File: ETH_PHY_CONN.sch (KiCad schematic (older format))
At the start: 65 parts, among them J2 RJMG2012211A0FR, U7 DP83869HMRGZT, Y1 XRCGE25M000FBA1AR0

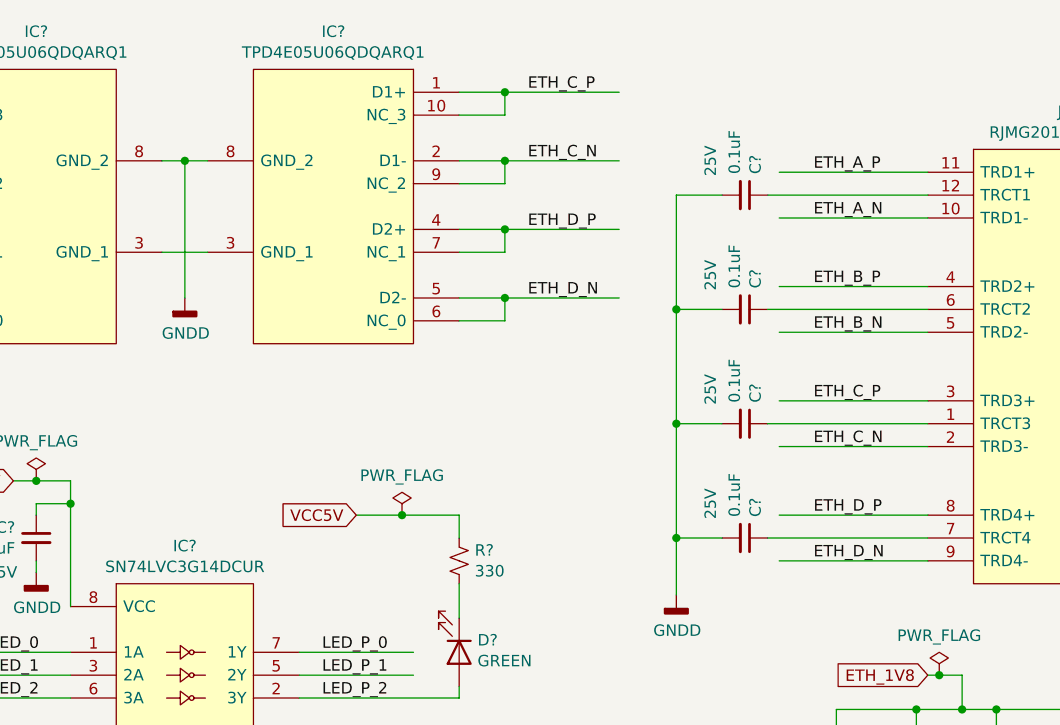
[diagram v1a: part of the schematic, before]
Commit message: Corrected Eth conn connections
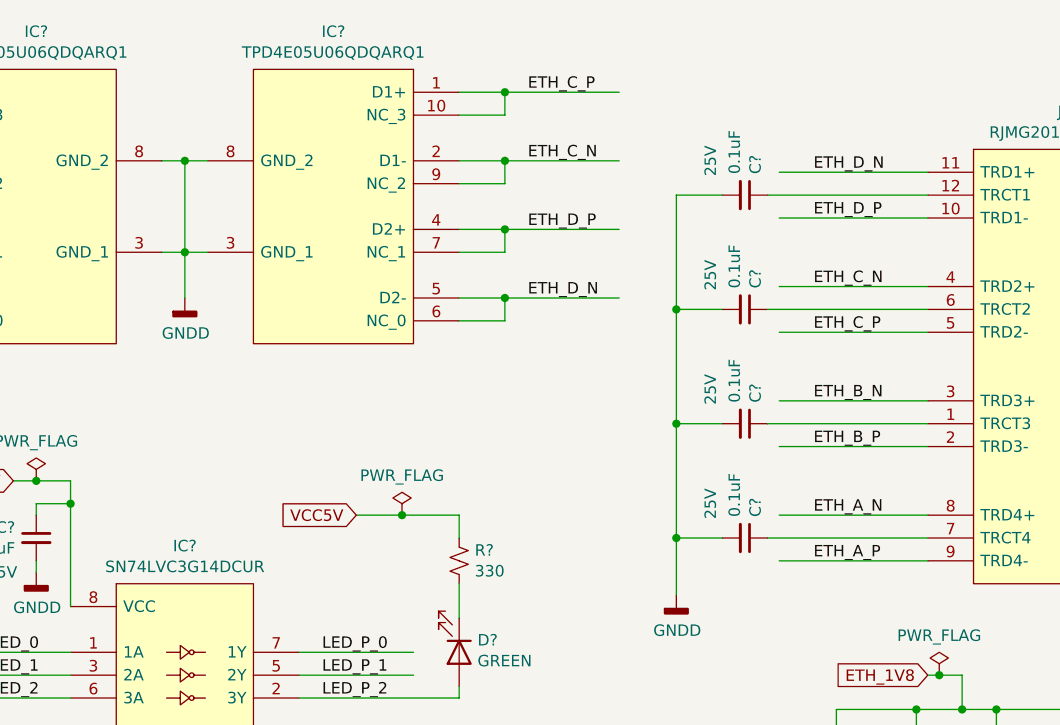
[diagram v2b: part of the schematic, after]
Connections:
- wire segments 304 -> 306

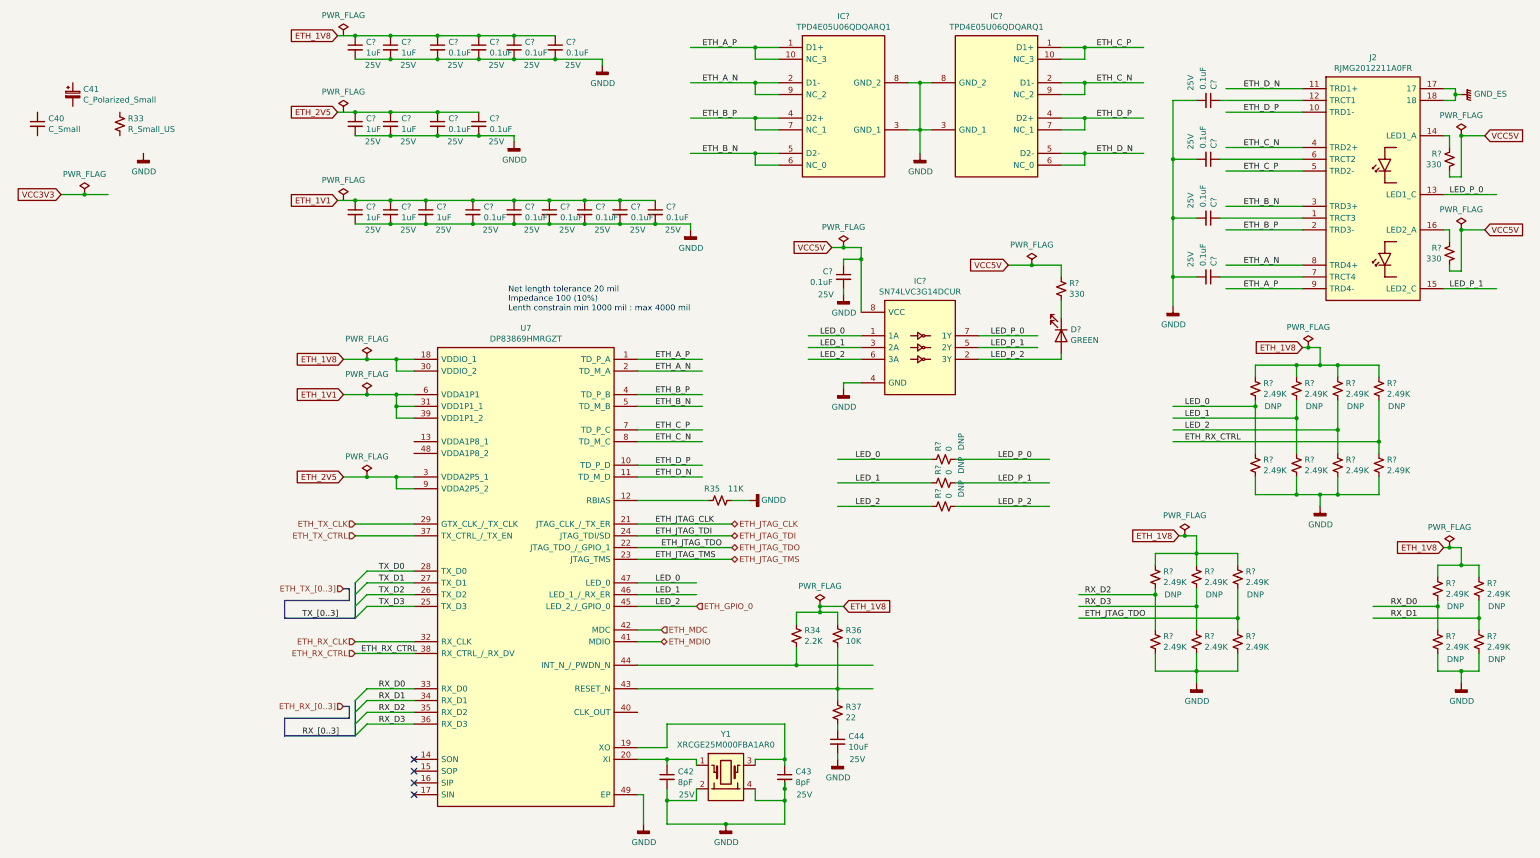
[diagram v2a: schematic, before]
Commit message: Modified LED nets and JTag nets of ETH schematic
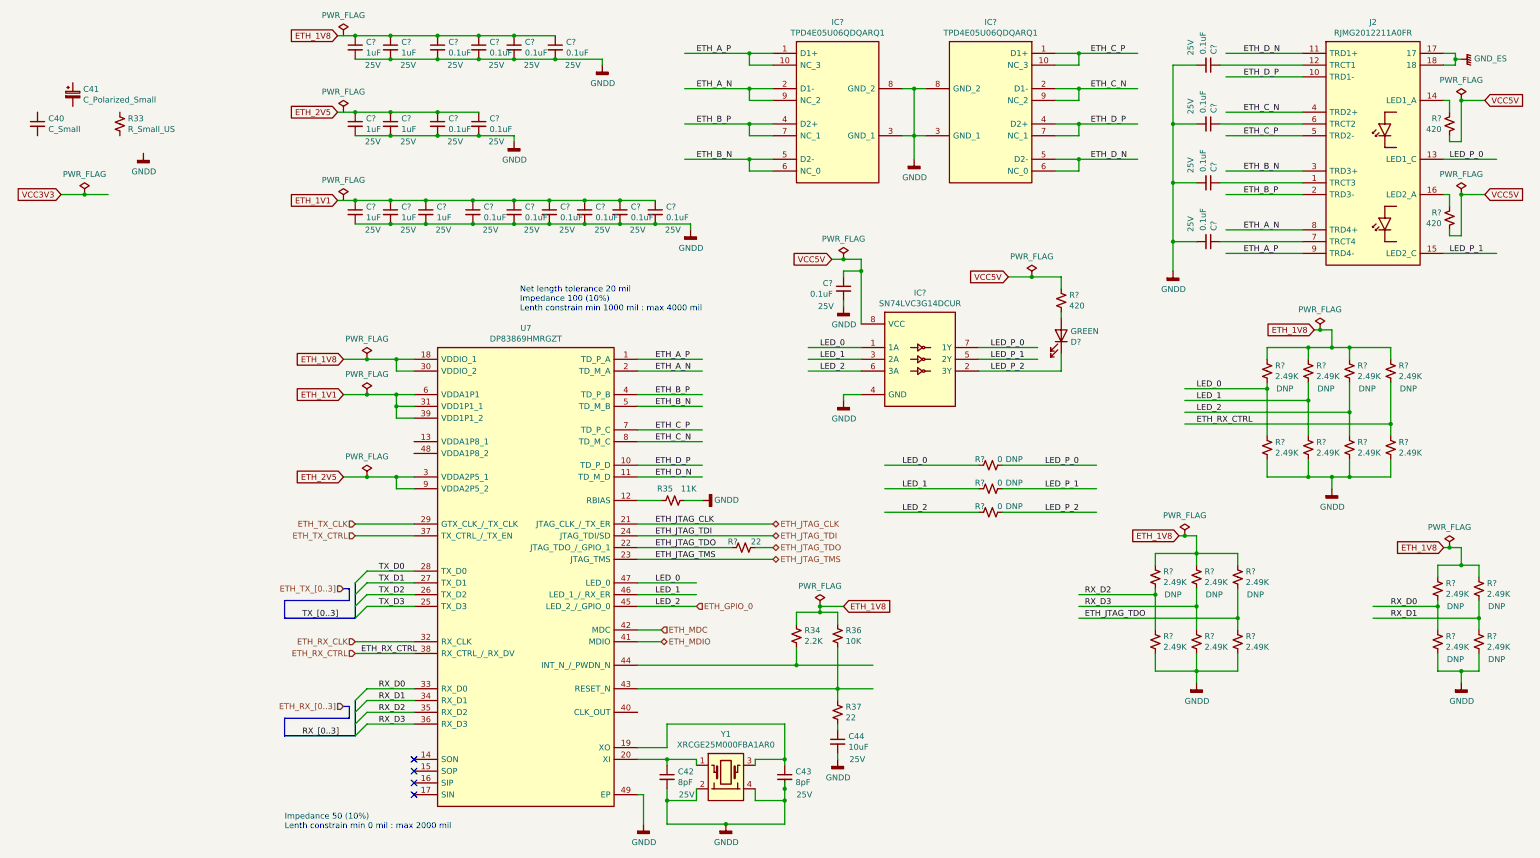
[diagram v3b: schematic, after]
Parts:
- added R?: 22, Resistor_SMD:R_0603_1608Metric_Pad0.98x0.95mm_HandSolder, symbol Device:R_Small_US
- R? (x3): value 330 -> 420
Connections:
- wire segments 306 -> 307
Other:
- note added: "Impedance 50 (10%)\nLenth constrain min 0 mil : max 2000 mil"
- moved on the sheet: C?, D?, IC?, J2, R35, R?

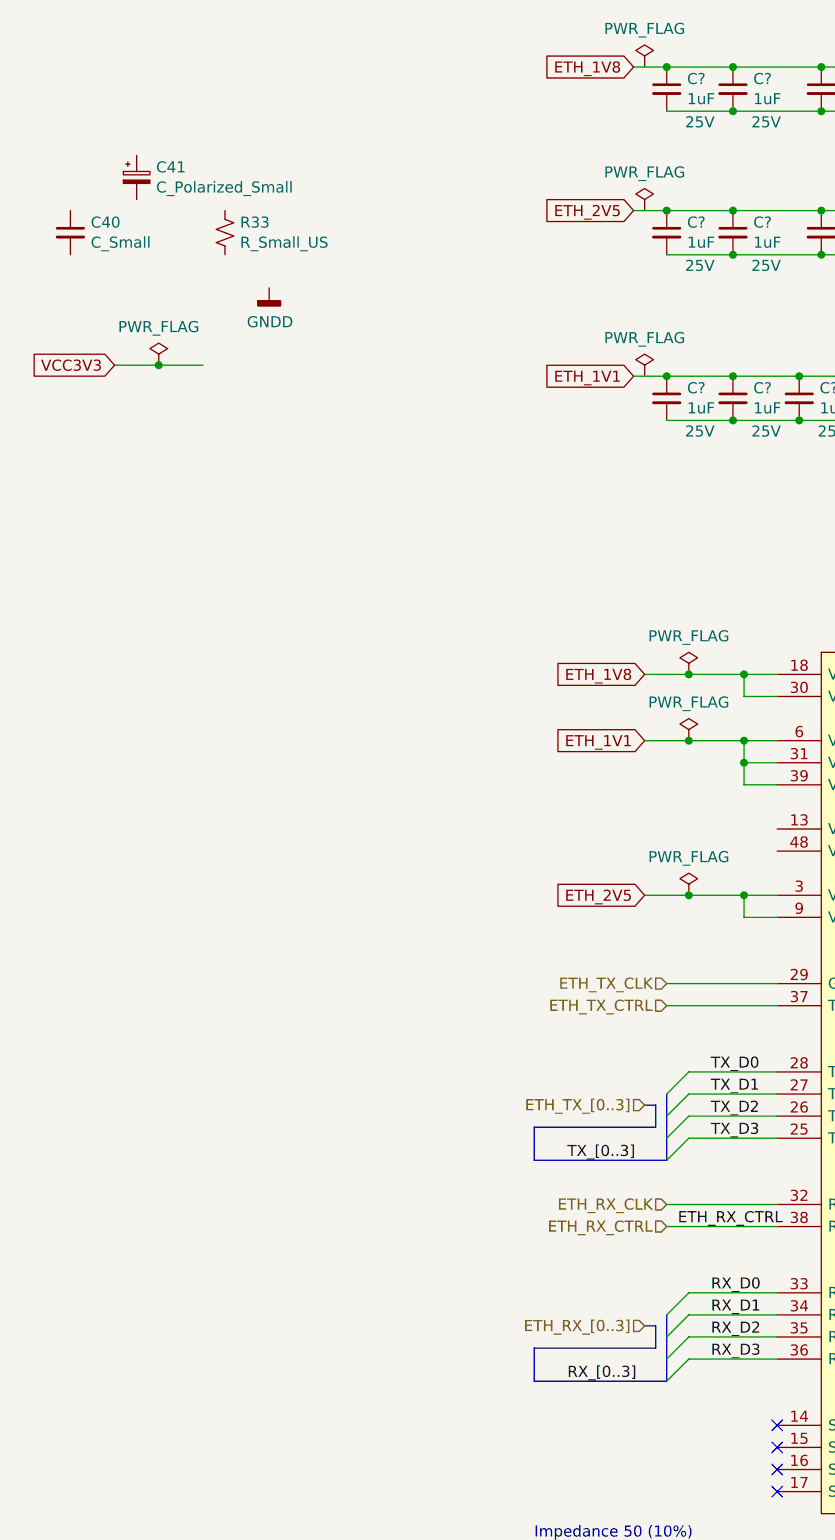
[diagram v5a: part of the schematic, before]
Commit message: Added bus lines -ETH_PHY_CONN -RAM -USB2 Made Output the port direction of clkout of Clock_Gen Placed sheet entris of sheet symbols on top sheet
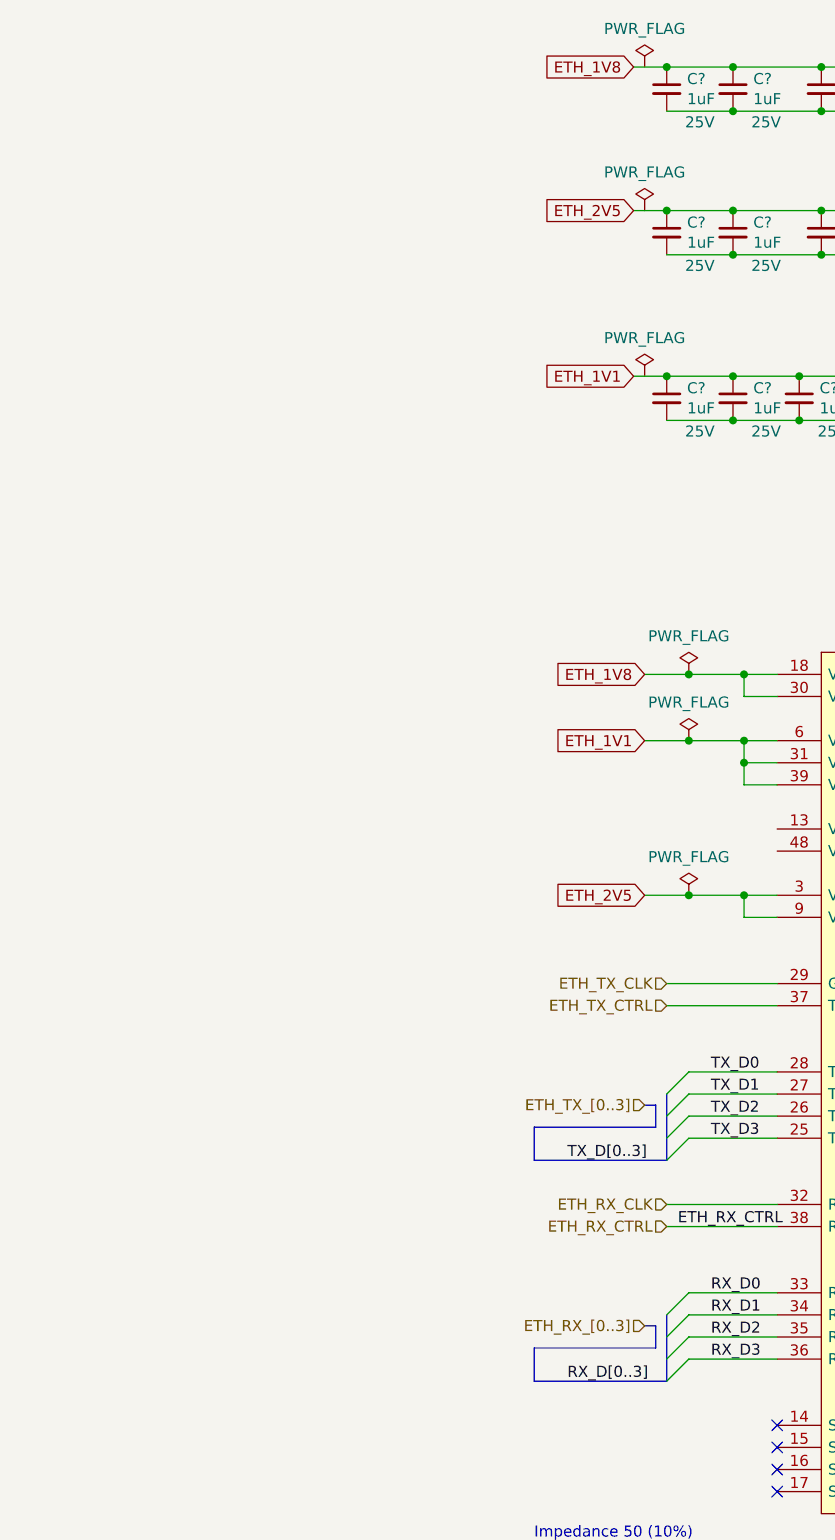
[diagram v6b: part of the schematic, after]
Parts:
- removed C40: C_Small, Capacitor_SMD:C_0603_1608Metric_Pad1.08x0.95mm_HandSolder, symbol Device:C_Small
- removed C41: C_Polarized_Small, Capacitor_Tantalum_SMD:CP_EIA-1608-10_AVX-L_Pad1.25x1.05mm_HandSolder, symbol Device:C_Polarized_Small
- removed R33: R_Small_US, Resistor_SMD:R_0603_1608Metric_Pad0.98x0.95mm_HandSolder, symbol Device:R_Small_US
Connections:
- net labels added: RX_D[0..3], TX_D[0..3]
- net labels removed: RX_[0..3], TX_[0..3], VCC3V3
- wire segments 307 -> 305
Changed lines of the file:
@@
 $Descr A4 11693 8268
 encoding utf-8
-Sheet 11 19
+Sheet 10 20
 Title ""
 Date ""
@@
 F 3 "http://www.ti.com/lit/gpn/DP83869HM" H 5450 2400 50  0001 L CNN
 	1    1900 3400
-	1    0    0    -1
-$EndComp
-$Comp
-L Device:R_Small_US R?
-U 1 1 6026D90E
-P -800 1500
-AR Path="/601E7C5A/6026D90E" Ref="R?"  Part="1"
-AR Path="/601E7CC8/6026D90E" Ref="R?"  Part="1"
-AR Path="/601E7C92/6026D90E" Ref="R?"  Part="1"
-AR Path="/601E7C92/60257FE5/6026D90E" Ref="R33"  Part="1"
-F 0 "R33" H -732 1546 50  0000 L CNN
-F 1 "R_Small_US" H -732 1455 50  0000 L CNN
-F 2 "Resistor_SMD:R_0603_1608Metric_Pad0.98x0.95mm_HandSolder" H -800 1500 50  0001 C CNN
-F 3 "~" H -800 1500 50  0001 C CNN
-	1    -800 1500
-	1    0    0    -1
-$EndComp
-$Comp
-L Device:C_Small C?
-U 1 1 6026D915
-P -1500 1500
-AR Path="/601E7C5A/6026D915" Ref="C?"  Part="1"
-AR Path="/601E7CC8/6026D915" Ref="C?"  Part="1"
-AR Path="/601E7C92/6026D915" Ref="C?"  Part="1"
-AR Path="/601E7C92/60257FE5/6026D915" Ref="C40"  Part="1"
-F 0 "C40" H -1408 1546 50  0000 L CNN
-F 1 "C_Small" H -1408 1455 50  0000 L CNN
-F 2 "Capacitor_SMD:C_0603_1608Metric_Pad1.08x0.95mm_HandSolder" H -1500 1500 50  0001 C CNN
-F 3 "~" H -1500 1500 50  0001 C CNN
-F 4 "" H -1500 1500 50  0000 C CNN "Voltage"
-	1    -1500 1500
-	1    0    0    -1
-$EndComp
-Text GLabel -1300 2100 0    50   Input ~ 0
-VCC3V3
-$Comp
-L power:PWR_FLAG #FLG?
-U 1 1 6026D91C
-P -1100 2100
-AR Path="/601E7C5A/6026D91C" Ref="#FLG?"  Part="1"
-AR Path="/601E7CC8/6026D91C" Ref="#FLG?"  Part="1"
-AR Path="/601E7C92/6026D91C" Ref="#FLG?"  Part="1"
-AR Path="/601E7C92/60257FE5/6026D91C" Ref="#FLG011"  Part="1"
-F 0 "#FLG011" H -1100 2175 50  0001 C CNN
-F 1 "PWR_FLAG" H -1100 2273 50  0000 C CNN
-F 2 "" H -1100 2100 50  0001 C CNN
-F 3 "~" H -1100 2100 50  0001 C CNN
-	1    -1100 2100
-	1    0    0    -1
-$EndComp
-Connection ~ -1100 2100
-Wire Wire Line
-	-1100 2100 -900 2100
-Wire Wire Line
-	-1300 2100 -1100 2100
-$Comp
-L power:GNDD #PWR?
-U 1 1 6026D925
-P -600 1750
-AR Path="/601DF0A6/6026D925" Ref="#PWR?"  Part="1"
-AR Path="/601E7C5A/6026D925" Ref="#PWR?"  Part="1"
-AR Path="/601E7CC8/6026D925" Ref="#PWR?"  Part="1"
-AR Path="/601E7C92/6026D925" Ref="#PWR?"  Part="1"
-AR Path="/601E7C92/60257FE5/6026D925" Ref="#PWR05"  Part="1"
-F 0 "#PWR05" H -600 1500 50  0001 C CNN
-F 1 "GNDD" H -596 1595 50  0000 C CNN
-F 2 "" H -600 1750 50  0001 C CNN
-F 3 "" H -600 1750 50  0001 C CNN
-	1    -600 1750
-	1    0    0    -1
-$EndComp
-$Comp
-L Device:C_Polarized_Small C?
-U 1 1 6026D92C
-P -1200 1250
-AR Path="/601E7C92/6026D92C" Ref="C?"  Part="1"
-AR Path="/601E7C92/60257FE5/6026D92C" Ref="C41"  Part="1"
-F 0 "C41" H -1112 1296 50  0000 L CNN
-F 1 "C_Polarized_Small" H -1112 1205 50  0000 L CNN
-F 2 "Capacitor_Tantalum_SMD:CP_EIA-1608-10_AVX-L_Pad1.25x1.05mm_HandSolder" H -1200 1250 50  0001 C CNN
-F 3 "~" H -1200 1250 50  0001 C CNN
-F 4 "" H -1200 1250 50  0000 C CNN "Voltage"
-	1    -1200 1250
 	1    0    0    -1
 $EndComp
@@
 ETH_TX_[0..3]
 Text Label 750  5700 0    50   ~ 0
-TX_[0..3]
+TX_D[0..3]
 Text HLabel 1200 5900 0    50   Input ~ 0
 ETH_RX_CLK
@@
 ETH_RX_[0..3]
 Text Label 750  6700 0    50   ~ 0
-RX_[0..3]
+RX_D[0..3]
 NoConn ~ 1700 6900
 NoConn ~ 1700 7000
